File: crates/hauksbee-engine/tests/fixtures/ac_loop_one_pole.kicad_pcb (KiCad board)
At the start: 2 parts, among them U1 AC_ERRAMP

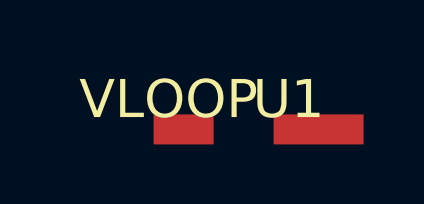
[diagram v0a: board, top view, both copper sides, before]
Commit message: Require explicit simple-regulator roles and reuse test fixtures
Simple voltage regulators now bind only with a finite output voltage and
distinct input, output and local-return nets, and stamp their source
between output and return. The AC-loop fixture drives its loop through the
dedicated supply source instead of a fake two-pin regulator. Shared CI run
configuration and evidence fixtures replace repeated test setup.

This does not yet make regulation conditional on input headroom.
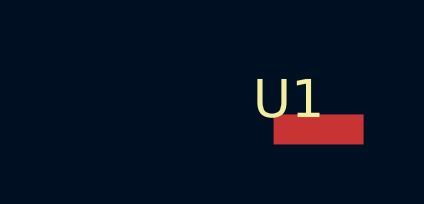
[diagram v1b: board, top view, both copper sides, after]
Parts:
- removed VLOOP: AC_LOOP_INJECTOR, Test:LoopInjector
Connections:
- U1 pad 2: FB -> +1V_VLOOP
- U1 pad 3: GND -> +1V_BIAS
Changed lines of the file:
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@@
   (net 0 "")
   (net 1 GND)
-  (net 2 FB)
+  (net 2 +1V_VLOOP)
   (net 3 OUT)
-  (module Test:LoopInjector (layer F.Cu)
-    (at 0 0)
-    (fp_text reference VLOOP (at 0 -1) (layer F.SilkS))
-    (fp_text value AC_LOOP_INJECTOR (at 0 1) (layer F.Fab))
-    (pad 1 smd rect (at 0 0) (size 1 1) (layers F.Cu)
-      (net 2 FB))
-    (pad 2 smd rect (at 1 0) (size 1 1) (layers F.Cu)
-      (net 1 GND))
-  )
+  (net 4 +1V_BIAS)
   (module Test:ErrorAmp (layer F.Cu)
     (at 4 0)
@@
       (net 3 OUT))
     (pad 2 smd rect (at 1 0) (size 1 1) (layers F.Cu)
-      (net 2 FB))
+      (net 2 +1V_VLOOP))
     (pad 3 smd rect (at 2 0) (size 1 1) (layers F.Cu)
-      (net 1 GND))
+      (net 4 +1V_BIAS))
   )
 )
